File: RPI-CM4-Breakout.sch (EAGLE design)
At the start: 26 parts, among them IC1 MC74VHC1G14DFT1G, J1 P1-100, J2 P101-200, J3 47571-0001

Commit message: Added USB block
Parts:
- removed JP1: JUMPER-SMT_2_NC_TRACE_NO-SILK, SparkFun-Jumpers:JUMPER-SMT_2_NC_TRACE_NO-SILK
- removed TP2: TEST-POINT3X5, SparkFun-Connectors:TEST-POINT3X5
- added C10, C11, C12, C13, C14, C9: 10uF, rcl:C-EUC0805
- added C15, C16, C17, C18, C19: 100nF, rcl:C-EUC0603
- added C5, C6: 27pF, rcl:C-EUC0603
- added C7: (no value), rcl:C-EUC0805
- added C8: 100uF, SparkFun-Capacitors:100UF-POLAR-EIA7343-16V-10%(TANT)
- added R10, R9: 12K, rcl:R-US_R0603
- added R11: 2K2, rcl:R-US_R0603
- added R12: 15K, rcl:R-US_R0603
- added R5, R6, R7, R8: 36K, rcl:R-US_R0603
- added TP8, TP9: TEST-POINT3X5, SparkFun-Connectors:TEST-POINT3X5
- added U1: USB2514B-I/M2, USB2514B-I_M2:USB2514B-I/M2
- added U2: FSUSB42MUX, FSUSB42MUX:FSUSB42MUX
- added U3: AP22653W6-7, AP22653W6-7:AP22653W6-7
- added U4: TPD4EUSB30DQAR, TPD4EUSB30DQAR:TPD4EUSB30DQAR
- added Y1: 24MHz, crystal:CRYSTALSM49
- J4: device SparkFun-Connectors:CONN_04SMD_RA_FEMALE -> EAGLE-INPUT_OUTPUT_CONNECTORS-rev17a:629104190121
- J5: value (none) -> 72309-8034BLF; device EAGLE-INPUT_OUTPUT_CONNECTORS-rev17a:629104190121 -> 72309-8034BLF:72309-8034BLF
- R2, R3: value 5.1k -> (none)
- renumbered CN1 to HDMI1
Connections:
- net N$10 renamed PCIE_NRST
- net N$100 renamed HDMI1_D0_P
- net N$102 renamed HDMI1_D0_N
- net N$106 renamed HDMI1_CK_P
- net N$108 renamed HDMI1_CK_N
- net N$11 renamed PCIE_CLK_P
- net N$129 renamed DSI1_C_N
- net N$13 renamed PCIE_CLK_N
- net N$131 renamed DSI1_C_P
- net N$135 renamed DSI1_D2_N
- net N$136 renamed DSI1_D3_N
- net N$137 renamed DSI1_D2_P
- net N$138 renamed DSI1_D3_P
- net N$20 renamed PCIE_RX_P
- net N$22 renamed PCIE_RX_N
- net N$25 renamed GPIO21
- net N$26 renamed GPIO19
- net N$27 renamed GPIO20
- net N$28 renamed GPIO13
- net N$29 renamed GPIO16
- net N$3 renamed PCIE_CLK_NREQ
- net N$30 renamed GPIO6
- net N$31 renamed GPIO12
- net N$33 renamed PCIE_TX_P
- net N$34 renamed GPIO5
- net N$35 renamed ID_SC
- net N$36 renamed ID_SD
- net N$37 renamed GPIO7
- net N$38 renamed GPIO11
- net N$39 renamed GPIO8
- net N$40 renamed GPIO9
- net N$41 renamed GPIO25
- net N$43 renamed PCIE_TX_N
- net N$44 renamed GPIO10
- net N$45 renamed GPIO24
- net N$46 renamed GPIO22
- net N$47 renamed GPIO23
- net N$48 renamed GPIO27
- net N$49 renamed GPIO18
- net N$50 renamed GPIO17
- net N$54 renamed GPIO4
- net N$56 renamed GPIO3
- net N$58 renamed CAM0_D0_N
- net N$60 renamed CAM0_D0_P
- net N$65 renamed CAM0_D1_N
- net N$67 renamed CAM0_D1_P
- net N$75 renamed CAM0_C_N
- net N$77 renamed CAM0_C_P
- net N$78 renamed HDMI1_HOTPLUG
- net N$80 renamed SCL0
- net N$81 renamed HDMI1_SDA
- net N$82 renamed SDA0
- net N$83 renamed HDMI1_D2_P
- net N$84 renamed HDMI1_SCL
- net N$85 renamed HDMI1_D2_N
- net N$86 renamed HDMI1_CEC
- net N$89 renamed WL_NDIS
- net N$90 renamed HDMI1_D1_P
- net N$91 renamed BT_NDIS
- net N$93 renamed HDMI1_D1_N
- removed net USBOTG_ID: J2.1, TP5.1
- new net HD1_N: J5.D-`, U1.USBDM_DN1/PRT_DIS_M1
- new net HD1_P: J5.D+`, U1.USBDP_DN1/PRT_DIS_P1
- new net HD2_N: J5.D-, U1.USBDM_DN2/PRT_DIS_M2
- new net HD2_P: J5.D+, U1.USBDP_DN2/PRT_DIS_P2
- new net N$10: R8.2, U1.SCL/CFG_SEL0/SMBCLK
- new net N$11: R9.1, U1.RBIAS
- new net N$13: C5.1, U1.XTALIN/CLKIN, Y1.1
- new net N$14: C6.1, U1.XTALOUT, Y1.2
- new net N$15: R10.1, R11.2, U2.SEL
- new net N$20: R12.2, U3.ILIM
- new net N$3: R5.2, U1.HS_IND/CFG_SEL1
- new net N$8: R6.2, U1.SUSP_IND/LOCAL_PWR/NON_REM0
- new net N$9: R7.2, U1.SDA/SMBDATA/NON_REM1
- new net NOCS1: U1.OCS_N1, U1.OCS_N2, U1.OCS_N3, U1.OCS_N4, U3.!FAULT
- new net PWR1: U1.PRTPWR1/BC_EN1, U3.EN
- new net USBD_N: J4.D+, U2.HSD2-, U4.D2+
- new net USBD_P: J4.D-, U2.HSD2+, U4.D2-
- new net USBH_N: U1.USBDM_UP, U2.HSD1-
- new net USBH_P: U1.USBDP_UP, U2.HSD1+
- new net USBOTG: J2.1, J4.VBUS, R11.1, TP5.1
- new net VBUS: C10.1, C11.1, C12.1, C8.+, C9.1, J5.VBUS, J5.VBUS`, U3.OUT
- net 3.3V: now also C13.1, C14.1, C15.1, C16.1, C17.1, C18.1, C19.1, U1.VBUS_DET, U1.VDD33, U1.VDDA33, U2.VCC; no longer J4.1, JP1.1
- net 5.0V: now also C7.1, U3.IN; no longer J5.VBUS
- net GND: now also C10.2, C11.2, C12.2, C13.2, C14.2, C15.2, C16.2, C17.2, C18.2, C19.2, C5.2, C6.2, C7.2, C8.-, C9.2, J4.GND, J4.SHIELD, J5.GND`, J5.S, R10.2, R12.1, R5.1, R6.1, R7.1, R8.1, R9.2, U1.VSS, U2.!OE, U2.GND, U3.GND, U4.GND_3; no longer J4.4, J5.SHIELD
- net GPIO14: no longer J4.3
- net GPIO15: no longer J4.2
- net GPIO_VREF: no longer JP1.2
- net N$6: now also TP8.1
- net N_EXTRST: now also TP9.1, U1.RESET_N; no longer TP2.1
- net USB2_N: now also U2.D-; no longer J5.D-
- net USB2_P: now also U2.D+; no longer J5.D+

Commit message: Initial layout
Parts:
- removed C1: 10uF, SparkFun-Capacitors:10UF-0603-6.3V-20%
- removed HDMI1: (no value), microbuilder:HDMI_MOLEX_47151-0001
- removed J3: 47571-0001, SamacSys_Parts:47571-0001
- removed TP6, TP7: TEST-POINT3X5, SparkFun-Connectors:TEST-POINT3X5
- added C20: (no value), rcl:C-EUC0603
- added C21: 10uF, SparkFun-Capacitors:10UF-0603-6.3V-20%
- added HDMI2: (no value), microbuilder:HDMI_MOLEX_47151-0001
- added J6: ARJM11A1-502-JJ-EW2, ARJM11A1-502-JJ-EW2:ARJM11A1-502-JJ-EW2
- added J7: 47571-0001, SamacSys_Parts:47571-0001
- added R13, R14: 470R, rcl:R-US_R0603
- added U5, U6: TPD4EUSB30DQAR, TPD4EUSB30DQAR:TPD4EUSB30DQAR
- C7: value (none) -> 10uF
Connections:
- new net CT: C20.1, J6.TRCT1, J6.TRCT2
- new net N$22: J6.L2, R13.1
- new net N$23: J6.L3, R14.2
- net 3.3V: now also C21.1, J6.L1, J6.L4, J7.VDD; no longer C1.1, J3.VDD
- net 5.0V: now also HDMI2G$1.+5V; no longer HDMI1G$1.+5V
- net ETH_LEDG: now also R13.2
- net ETH_LEDY: now also R14.1
- net GND: now also C20.2, C21.2, HDMI2G$1.GND, HDMI2G$1.TX0_SHIELD, HDMI2G$1.TX1_SHIELD, HDMI2G$1.TX2_SHIELD, HDMI2G$1.TXC_SHIELD, J7.GND, J7.SHIELD; no longer C1.2, HDMI1G$1.GND, HDMI1G$1.TX0_SHIELD, HDMI1G$1.TX1_SHIELD, HDMI1G$1.TX2_SHIELD, HDMI1G$1.TXC_SHIELD, J3.GND, J3.SHIELD
- net GPIO14: no longer TP7.1
- net GPIO15: no longer TP6.1
- net HDMI0_CK_N: now also HDMI2G$1.TXC-; no longer HDMI1G$1.TXC-
- net HDMI0_CK_P: now also HDMI2G$1.TXC+; no longer HDMI1G$1.TXC+
- net HDMI0_D0_N: now also HDMI2G$1.TX0-; no longer HDMI1G$1.TX0-
- net HDMI0_D0_P: now also HDMI2G$1.TX0+; no longer HDMI1G$1.TX0+
- net HDMI0_D1_N: now also HDMI2G$1.TX1-; no longer HDMI1G$1.TX1-
- net HDMI0_D1_P: now also HDMI2G$1.TX1+; no longer HDMI1G$1.TX1+
- net HDMI0_D2_N: now also HDMI2G$1.TX2-; no longer HDMI1G$1.TX2-
- net HDMI0_D2_P: now also HDMI2G$1.TX2+; no longer HDMI1G$1.TX2+
- net HDMI0_HOTPLUG: now also HDMI2G$1.HOTPLUG; no longer HDMI1G$1.HOTPLUG
- net HDMI0_SCL: now also HDMI2G$1.DCLK; no longer HDMI1G$1.DCLK
- net HDMI0_SDA: now also HDMI2G$1.DDAT; no longer HDMI1G$1.DDAT
- net NOCS1: no longer U1.OCS_N3, U1.OCS_N4
- net SD_CLK: now also J7.CLK; no longer J3.CLK
- net SD_CMD: now also J7.CMD; no longer J3.CMD
- net SD_DAT0: now also J7.DAT0; no longer J3.DAT0
- net SD_DAT1: now also J7.DAT1; no longer J3.DAT1
- net SD_DAT2: now also J7.DAT2; no longer J3.DAT2
- net SD_DAT3: now also J7.CD/DAT3; no longer J3.CD/DAT3
- net TRD0_N: now also J6.TRD1-, U6.D1-
- net TRD0_P: now also J6.TRD1+, U6.D1+
- net TRD1_N: now also J6.TRD2-, U6.D2+
- net TRD1_P: now also J6.TRD2+, U6.D2-
- net TRD2_N: now also J6.TRD3-, U5.D1-
- net TRD2_P: now also J6.TRD3+, U5.D1+
- net TRD3_N: now also J6.TRD4-, U5.D2+
- net TRD3_P: now also J6.TRD4+, U5.D2-

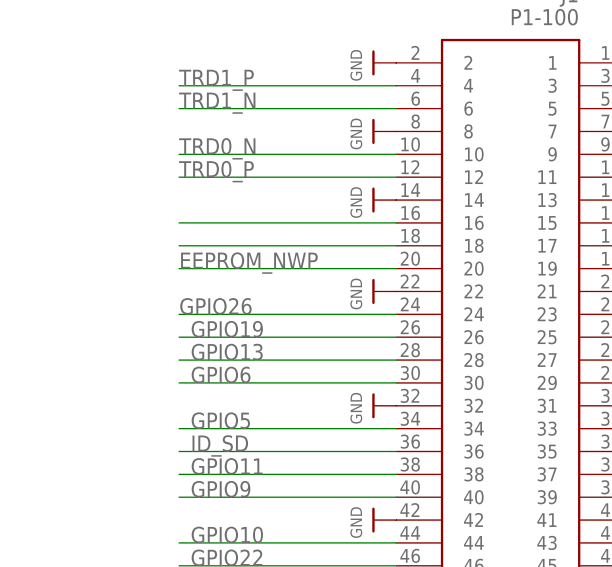
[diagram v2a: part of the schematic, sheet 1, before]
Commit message: Moved CM4 to bottom side
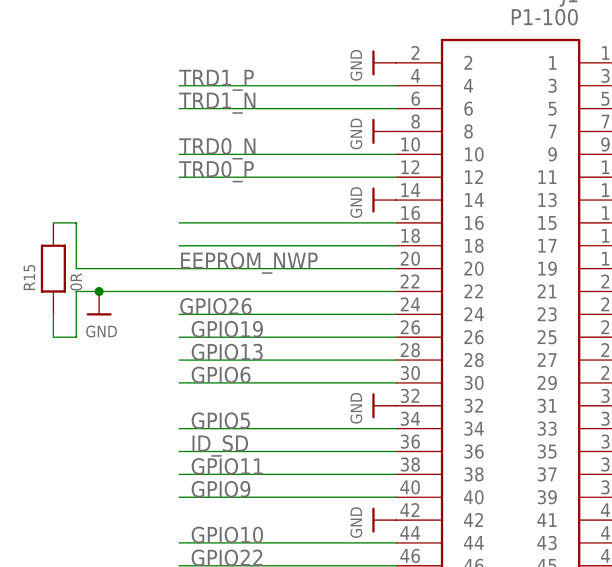
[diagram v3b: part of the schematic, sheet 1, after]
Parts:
- added R15: 0R, microbuilder:RESISTOR_0402MP
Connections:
- net EEPROM_NWP: now also R15.2
- net GND: now also R15.1
